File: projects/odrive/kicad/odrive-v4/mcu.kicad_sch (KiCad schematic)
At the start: 20 parts, among them J4 FTSH-105-01-L-DV-K, U16 TPD4E05U06, U2 STM32F405RGT6, Y1 8MHz

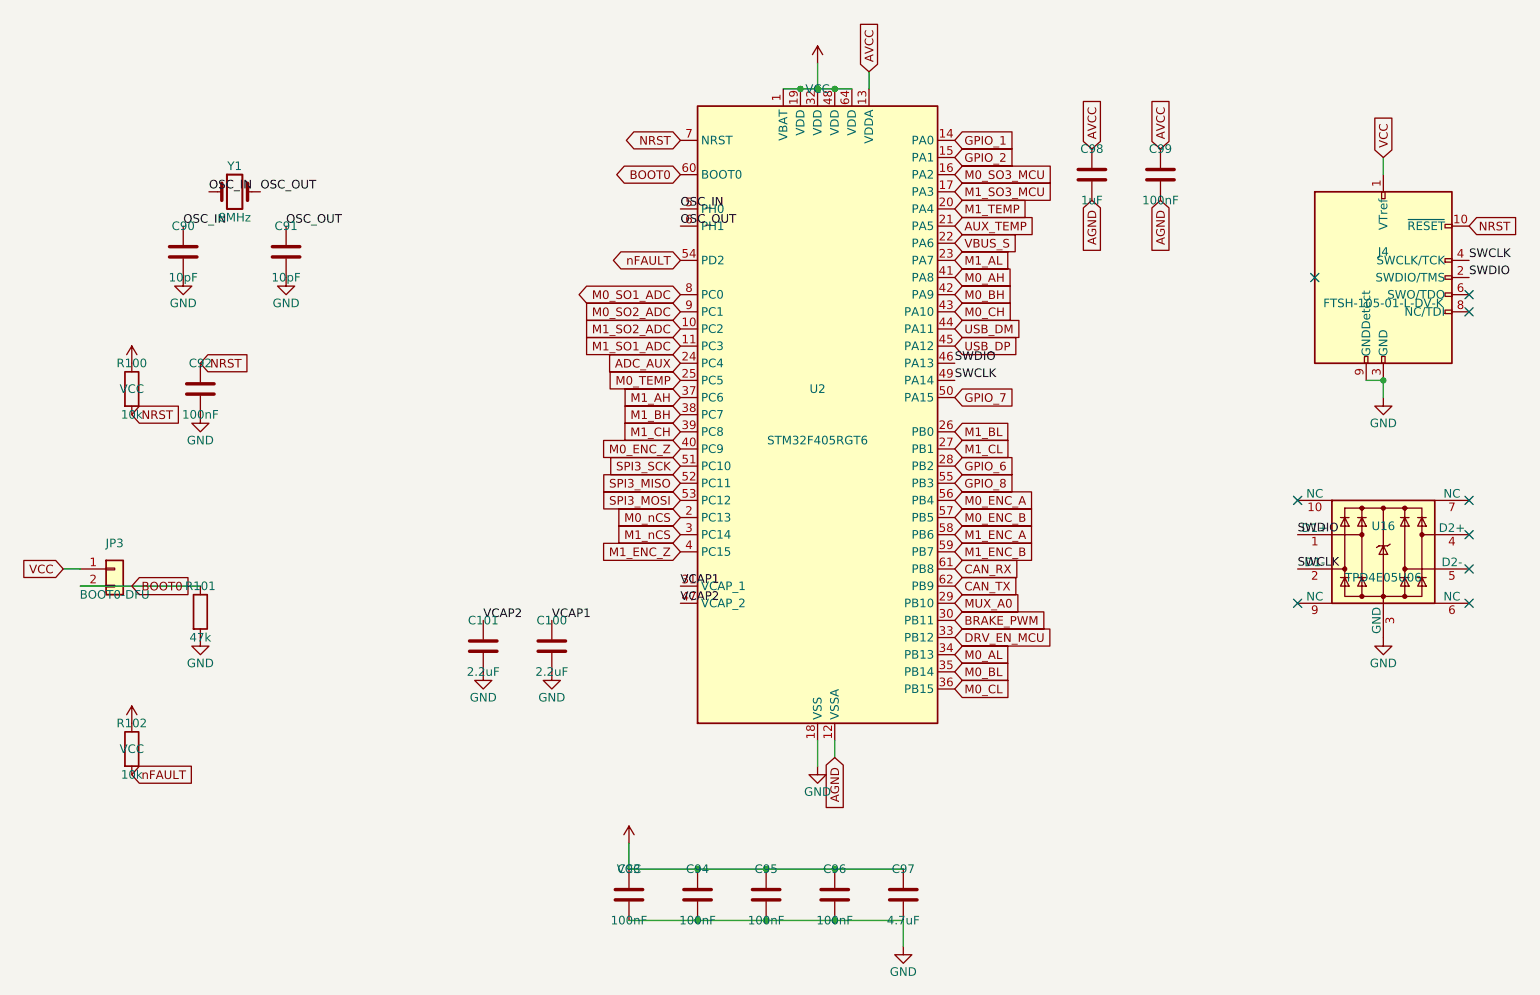
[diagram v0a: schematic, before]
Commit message: Make the v4 schematic sheets readable, netlist-invariant
The verified v4 schematic was electrically perfect and visually unreadable:
connectivity lived in labels stuck on pins, text overlapped, and parts sat
on the title block. Reworked all ten block sheets through Konnect: real
wires for local connections, labels kept for power rails and inter-sheet
nets, parts grouped by function, junction dots where wires join.

The invariant was enforced, not assumed: the exported netlist is diffed
against a reference frozen before the rework - 378 components and 283 nets,
identical membership pin by pin - and ERC holds at 0 errors. The lesson
that forced the rework is now a standing gate: numeric oracles (ERC,
netlist diff, overlap counts) all passed on the unreadable version, so
every sheet is also rendered to PNG and looked at before being declared
done.

An interrupted fix round left one known cosmetic issue, documented in
docs/LOG.md: the encoders-gpio GPIO group's reference/value text fields
float ~134mm right of their symbols, over the title block. konnect 0.2.2
has no tool that repositions property fields, so it waits for 0.11.0.
Also adds the fab footprints the sheets reference (MEGA fuse, Phoenix
terminal blocks, CMC) and restores the board file to the blank template -
the aborted layout skeleton was not worth keeping.
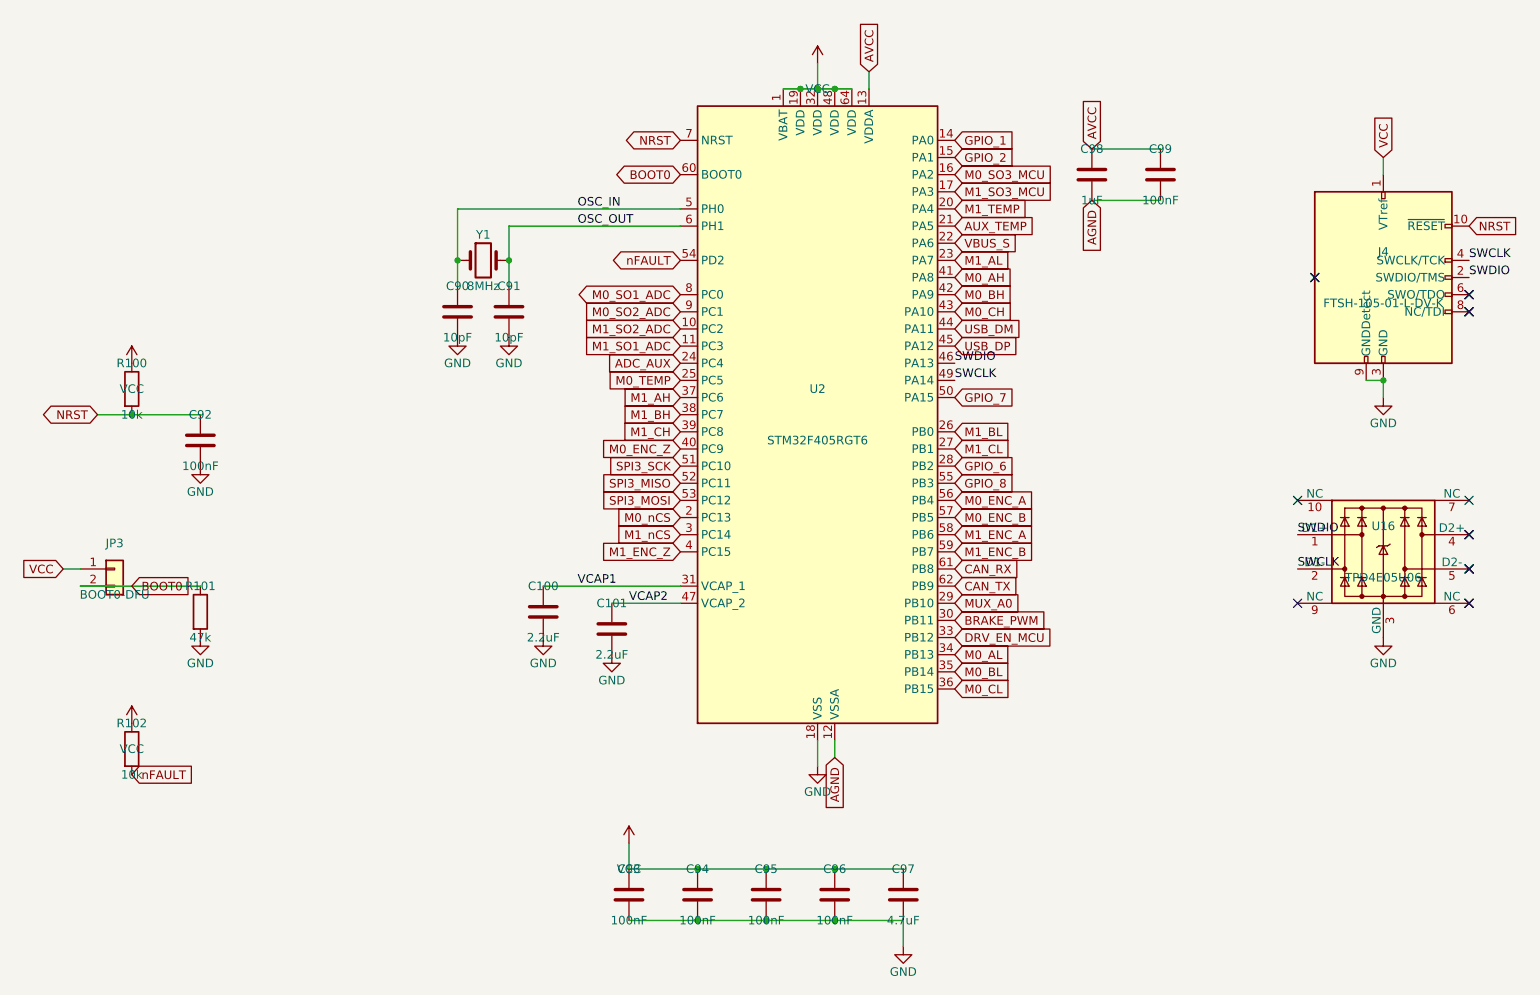
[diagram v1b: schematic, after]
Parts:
- C100, C101, C90, C91, C92, C93, C94, C95, C96, C98, C99: footprint (none) -> Capacitor_SMD:C_0603_1608Metric
- C97: footprint (none) -> Capacitor_SMD:C_0805_2012Metric
- J4: footprint (none) -> Connector_PinHeader_1.27mm:PinHeader_2x05_P1.27mm_Vertical_SMD
- JP3: footprint (none) -> Connector_PinHeader_2.54mm:PinHeader_1x02_P2.54mm_Vertical
- R100, R101, R102: footprint (none) -> Resistor_SMD:R_0603_1608Metric
- U16: footprint (none) -> Package_SON:USON-10_2.5x1.0mm_P0.5mm
- U2: footprint (none) -> Package_QFP:LQFP-64_10x10mm_P0.5mm
- Y1: footprint (none) -> Crystal:Crystal_SMD_5032-2Pin_5.0x3.2mm
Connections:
- no-connect marks 9 -> 15
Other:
- moved on the sheet: C100, C101, C90, C91, C92, Y1
